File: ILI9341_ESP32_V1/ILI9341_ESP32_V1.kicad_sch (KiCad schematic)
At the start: 73 parts, among them J1 USB_C_Receptacle_USB2.0_16P, J10 Conn_01x01_Pin, J4 Conn_01x18_Socket, J7 Conn_01x18_Socket, J9 Conn_01x01_Pin, Q1 BC817, Q2 BC817, Q4 BC817, SW1 SW_DIP_x01, SW13 SW_Wuerth_450301014042, SW7 SW_Push, SW8 SW_Push, U1 HE6250xx, U10 CH340K, U11 ESP32-WROVER-E-N8R8, U2 XM5062S, U4 MAX98357AETE+T, U7 02FVS3

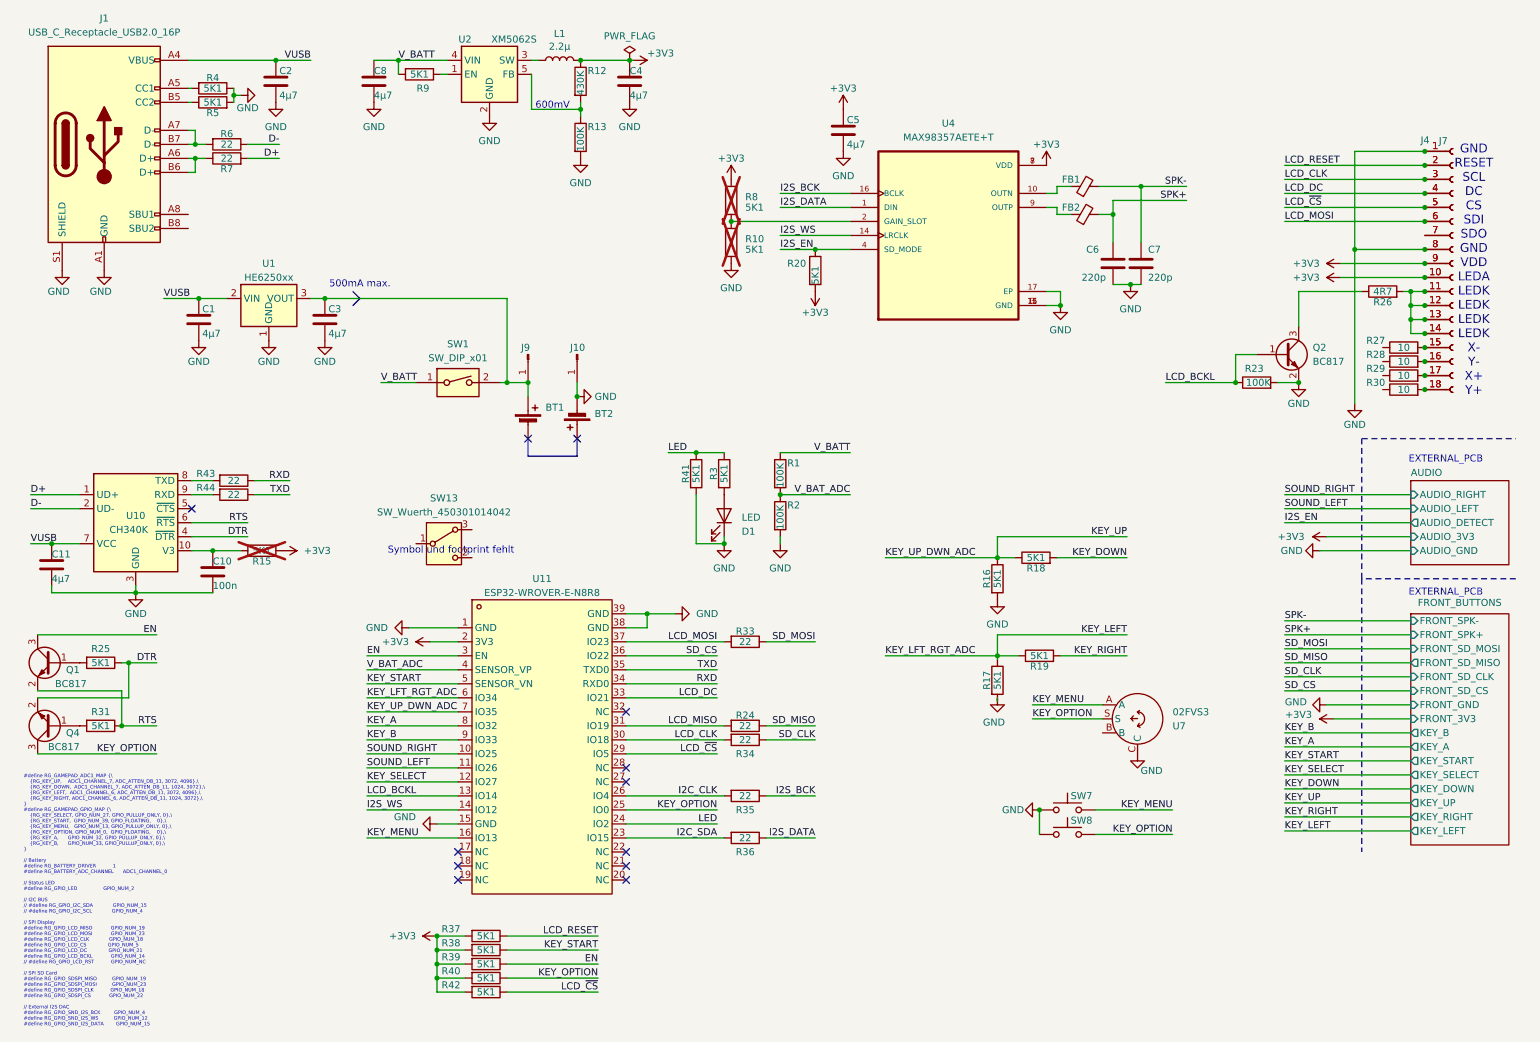
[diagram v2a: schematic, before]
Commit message: update cardridge grabber funktion
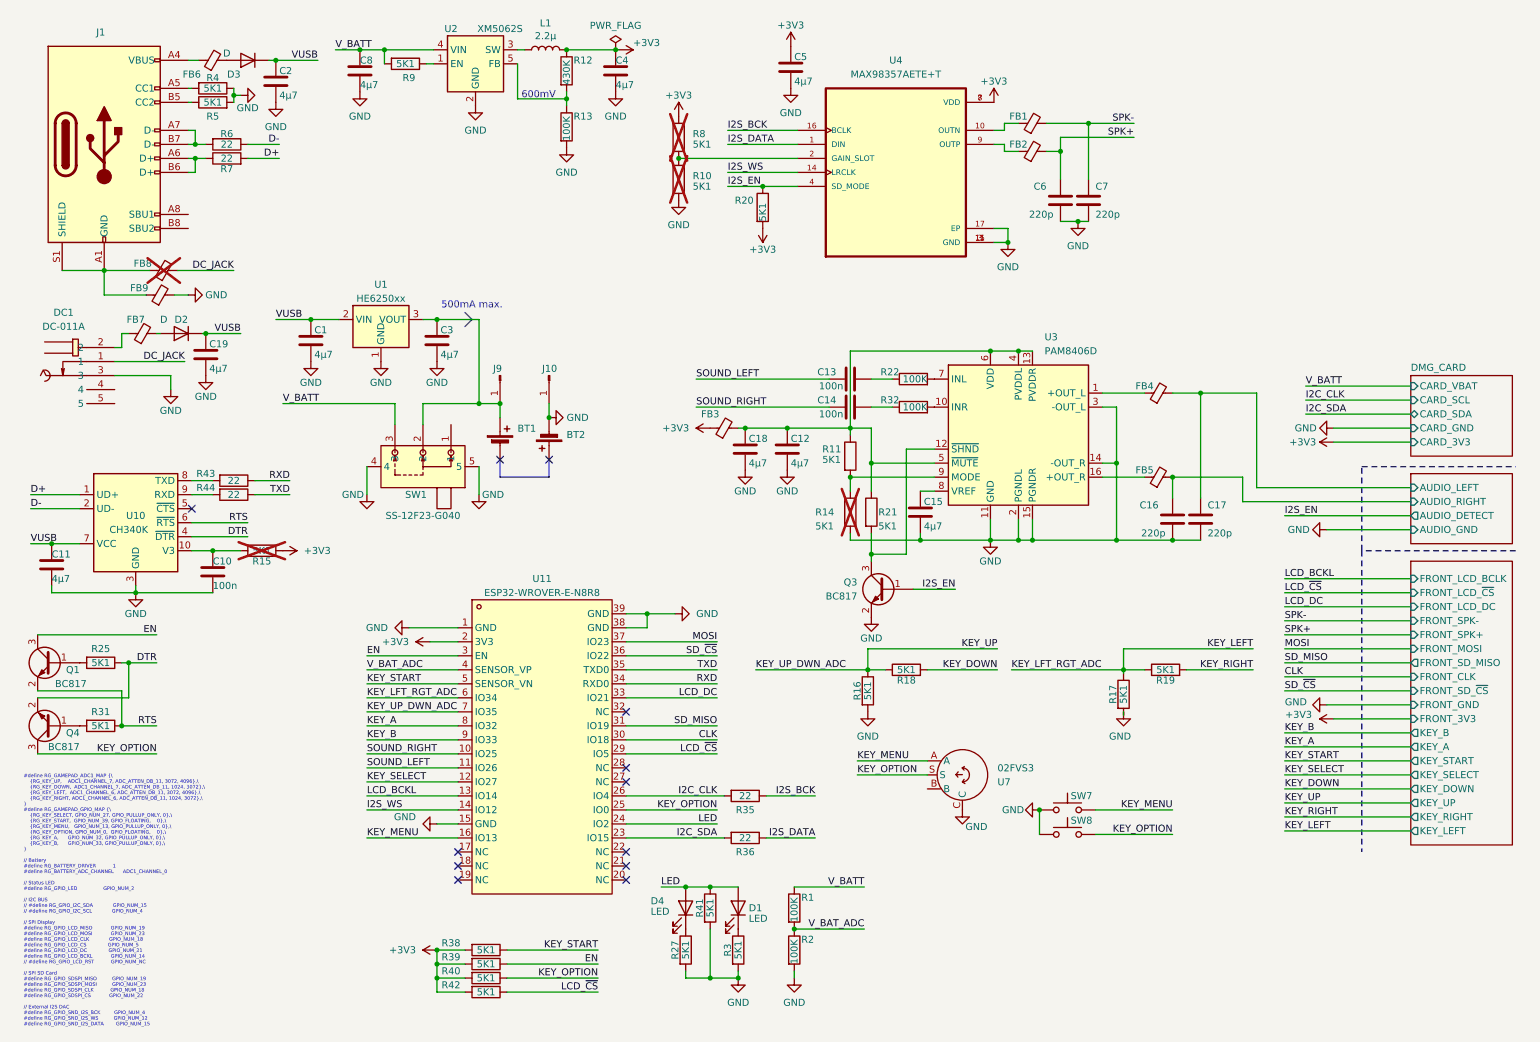
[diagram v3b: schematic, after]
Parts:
- removed J4, J7: Conn_01x18_Socket, TheBrutzlers_Lib:solder connector 0.8mm 18 pin, symbol Connector:Conn_01x18_Socket
- removed Q2: BC817, Package_TO_SOT_SMD:SOT-23, symbol Transistor_BJT:BC817
- removed R23: 100K, Resistor_SMD:R_0603_1608Metric_Pad0.98x0.95mm_HandSolder, symbol Device:R
- removed R24, R33, R34: 22, Resistor_SMD:R_0603_1608Metric_Pad0.98x0.95mm_HandSolder, symbol Device:R
- removed R26: 4R7, Resistor_SMD:R_0603_1608Metric_Pad0.98x0.95mm_HandSolder, symbol Device:R
- removed R28, R29, R30: 10, Resistor_SMD:R_0603_1608Metric_Pad0.98x0.95mm_HandSolder, symbol Device:R
- removed R37: 5K1, Resistor_SMD:R_0603_1608Metric_Pad0.98x0.95mm_HandSolder, symbol Device:R
- removed SW1: SW_DIP_x01, Button_Switch_SMD:SW_SPDT_PCM12, symbol Switch:SW_DIP_x01
- removed SW13: SW_Wuerth_450301014042, Button_Switch_THT:SW_Slide-03_Wuerth-WS-SLTV_10x2.5x6.4_P2.54mm, symbol Switch:SW_Wuerth_450301014042
- added C12, C15, C18, C19: 4µ7, Capacitor_SMD:C_1206_3216Metric, symbol Device:C
- added C13, C14: 100n, Capacitor_SMD:C_1206_3216Metric, symbol Device:C
- added C16, C17: 220p, Capacitor_SMD:C_0603_1608Metric, symbol Device:C
- added D2, D3: D, Diode_SMD:Nexperia_CFP3_SOD-123W, symbol Device:D
- added D4: LED, LED_SMD:LED_0603_1608Metric, symbol Device:LED
- added DC1: DC-011A, easyeda2kicad:DC-IN-TH_DC-011A, symbol easyeda2kicad:DC-011A
- added FB3, FB4, FB5, FB6, FB7, FB8, FB9: FerriteBead_Small, Inductor_SMD:L_0805_2012Metric, symbol Device:FerriteBead_Small
- added Q3: BC817, Package_TO_SOT_SMD:SOT-323_SC-70, symbol Transistor_BJT:BC817
- added R11, R14, R21: 5K1, Resistor_SMD:R_0603_1608Metric, symbol Device:R
- added R22, R32: 100K, Resistor_SMD:R_0603_1608Metric_Pad0.98x0.95mm_HandSolder, symbol Device:R
- added SW1: SS-12F23-G040, easyeda2kicad:SW-TH_SS-12F23-G040, symbol easyeda2kicad:SS-12F23-G040
- added U3: PAM8406D, Package_SO:SOP-16_3.9x9.9mm_P1.27mm, symbol Amplifier_Audio:PAM8406D
- Q1, Q4: footprint Package_TO_SOT_SMD:SOT-23 -> Package_TO_SOT_SMD:SOT-323_SC-70; LCSC (none) -> C383187
- R27: value 10 -> 5K1
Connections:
- net LCD_MISO is gone; now on net SD_MISO: U11.31 (IO19)
- net +3V3: now also FB3.1
- net GND: now also R27.2, R3.2, C12.2, C15.2, C16.2, C17.1, C18.2, C19.2, DC1.3, FB9.2, Q3.2 (E), R14.2, SW1.4, SW1.5, U3.11 (GND), U3.14 (-OUT_R), U3.15 (PGNDR), U3.2 (PGNDL), U3.3 (-OUT_L); no longer D1.1 (K), J1.A1 (GND), J1.A12 (GND), J1.B1 (GND), J1.B12 (GND), J1.S1 (SHIELD)
- net I2S_EN: now also Q3.1 (B)
- net LED: now also D1.2 (A), D4.2 (A); no longer R3.1
- net SOUND_LEFT: now also C13.1
- net SOUND_RIGHT: now also C14.1
- net VUSB: now also C19.1, D2.1 (K), D3.1 (K); no longer J1.A4 (VBUS), J1.A9 (VBUS), J1.B4 (VBUS), J1.B9 (VBUS)
- net V_BATT: now also SW1.3
- net at BT1.1 (+), C3.1, J9.1 (Pin_1)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: now also SW1.2
- net at R27.1: now also D4.1 (K)
- net LCD_CLK renamed CLK
- net LCD_MOSI renamed MOSI
- net SD_CS renamed SD_~{CS}
- new net: D1.1 (K), R3.1
- new net: DC1.2, FB7.1
- new net: C12.1, C18.1, FB3.2, R11.1, R21.1, U3.13 (PVDDR), U3.4 (PVDDL), U3.5 (~{MUTE}), U3.6 (VDD)
- new net: R11.2, R14.1, U3.9 (MODE)
- new net: D2.2 (A), FB7.2
- new net: Q3.3 (C), R21.2, U3.12 (~{SHND})
- new net: FB5.1, U3.16 (+OUT_R)
- new net: C14.2, R32.1
- new net: R32.2, U3.10 (INR)
- new net: FB8.1, FB9.1, J1.A1 (GND), J1.A12 (GND), J1.B1 (GND), J1.B12 (GND), J1.S1 (SHIELD)
- new net: C13.2, R22.1
- new net: C15.1, U3.8 (VREF)
- new net: D3.2 (A), FB6.2
- new net: R22.2, U3.7 (INL)
- new net: FB4.1, U3.1 (+OUT_L)
- new net: FB6.1, J1.A4 (VBUS), J1.A9 (VBUS), J1.B4 (VBUS), J1.B9 (VBUS)
- new net AUDIO/AUDIO_LEFT: C17.2, FB4.2
- new net AUDIO/AUDIO_RIGHT: C16.1, FB5.2
- new net DC_JACK: DC1.1, FB8.2
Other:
- added sheet DMG_CARD (untitled.kicad_sch)
- sheet AUDIO ports: added none; removed AUDIO_3V3
- sheet FRONT_BUTTONS ports: added FRONT_CLK, FRONT_LCD_BCLK, FRONT_LCD_DC, FRONT_LCD_~{CS}, FRONT_MOSI, FRONT_SD_~{CS}; removed FRONT_SD_CLK, FRONT_SD_CS, FRONT_SD_MOSI
- note removed: "EXTERNAL_PCB"
- note removed: "GND RESET SCL DC CS SDI SDO GND VDD LEDA LEDK LEDK LEDK LEDK X- Y- X+ Y+"
- note removed: "Symbol und footprint fehlt"
- moved on the sheet: BT1, BT2, C1, C3, C4, C5, C6, C7, C8, D1, FB1, FB2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

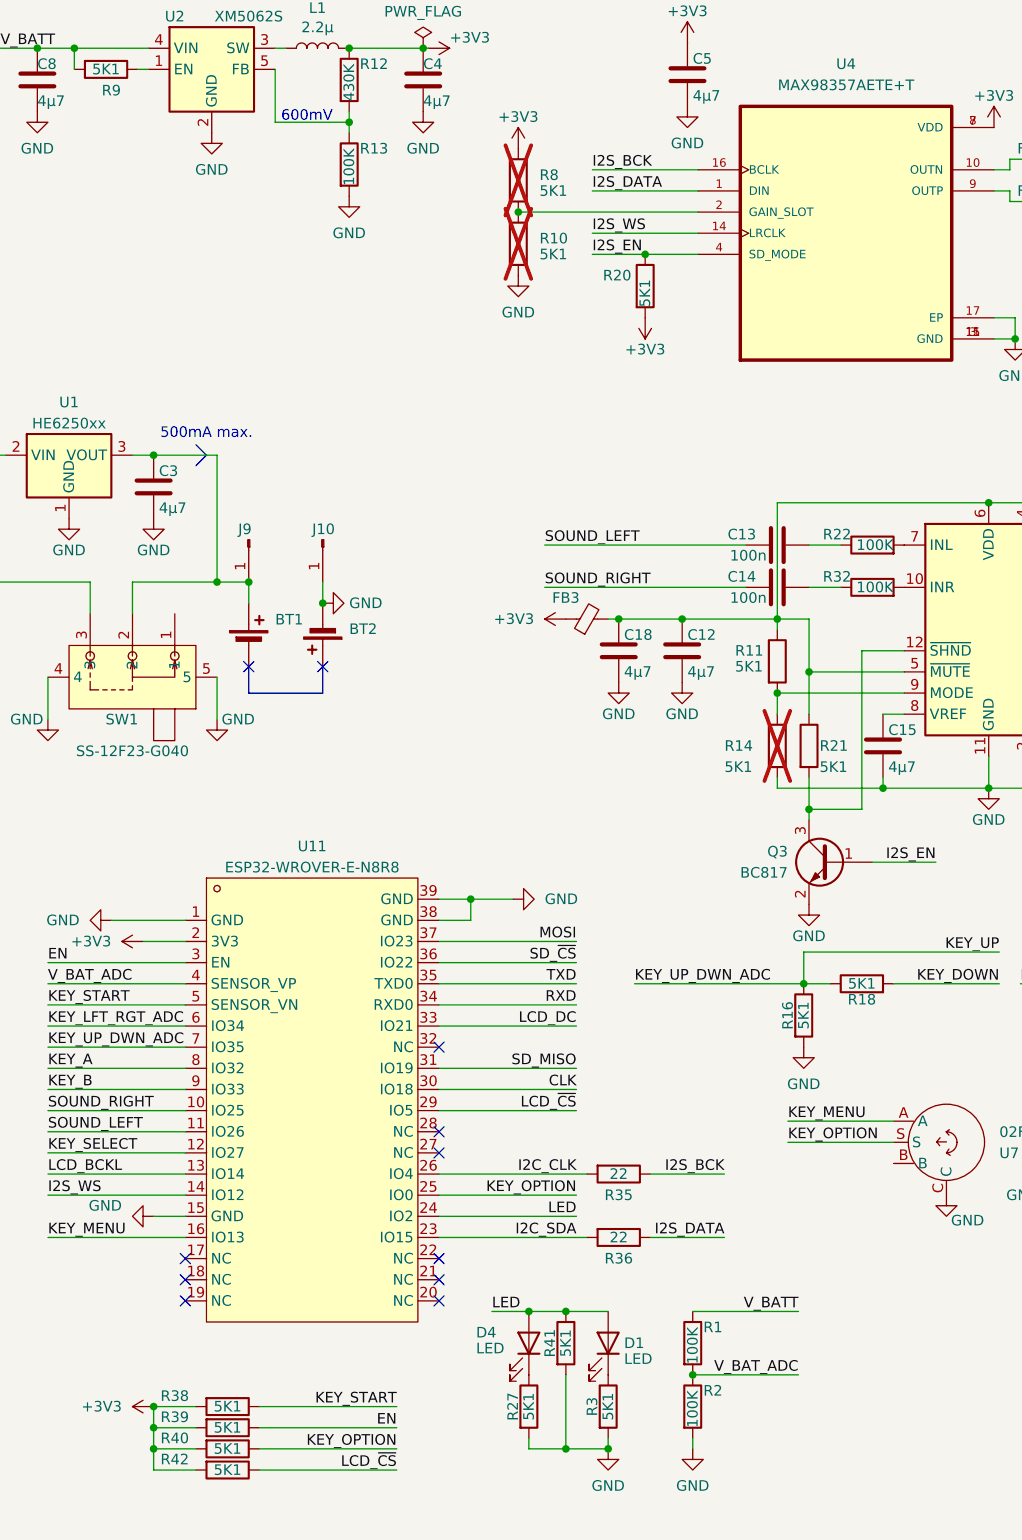
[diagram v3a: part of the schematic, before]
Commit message: update routing and put display on front pcb
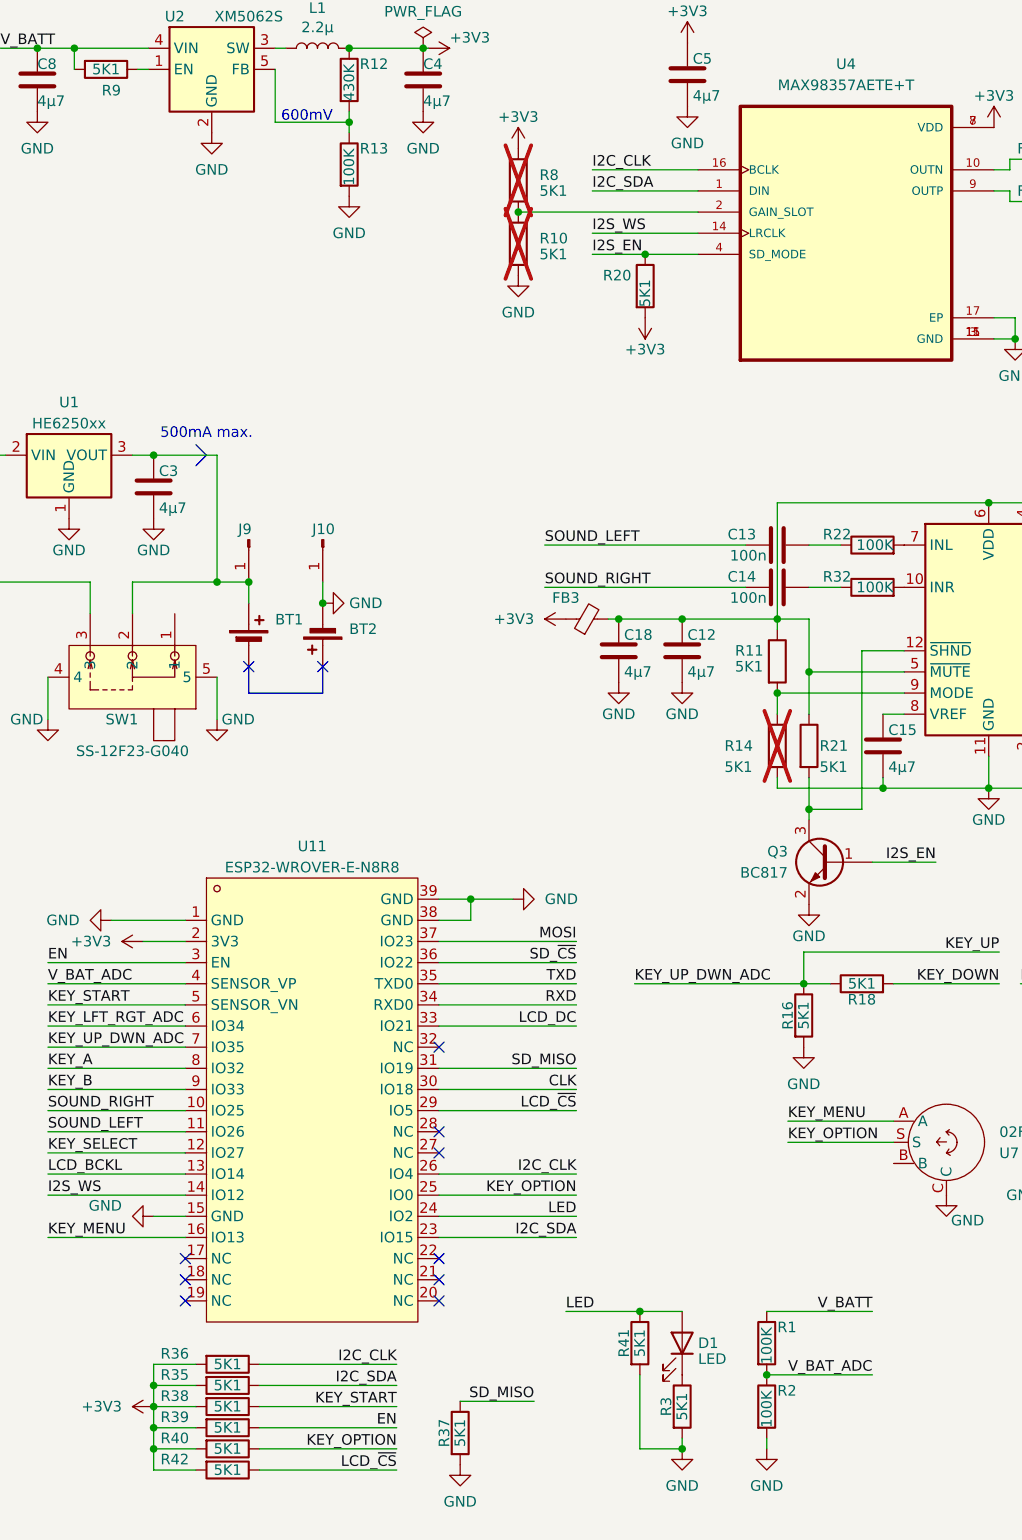
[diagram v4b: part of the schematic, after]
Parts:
- removed D4: LED, LED_SMD:LED_0603_1608Metric, symbol Device:LED
- removed R27: 5K1, Resistor_SMD:R_0603_1608Metric_Pad0.98x0.95mm_HandSolder, symbol Device:R
- added R37: 5K1, Resistor_SMD:R_0603_1608Metric_Pad0.98x0.95mm_HandSolder, symbol Device:R
- R35, R36: value 22 -> 5K1
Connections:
- net +3V3: now also R35.2, R36.2
- net GND: now also R37.2
- net I2C_CLK: now also R36.1, U4.16 (BCLK); no longer R35.2
- net I2C_SDA: now also R35.1, U4.1 (DIN); no longer R36.2
- net SD_MISO: now also R37.1
- removed net I2S_BCK: R35.1, U4.16 (BCLK)
- removed net I2S_DATA: R36.1, U4.1 (DIN)
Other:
- moved on the sheet: D1, R1, R2, R3, R41
